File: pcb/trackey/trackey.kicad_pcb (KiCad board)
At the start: 2 copper layers, 53.3 x 58.4 mm, 31 parts, among them J1 trackball_port, J2 Audio-Jack-4, J3 COL_port, J4 ROW_port, J6 has_trackball, J7 is_left, U1 Arduino_Pro_Micro, U2 Arduino_Pro_Micro, U3 MCP23S17

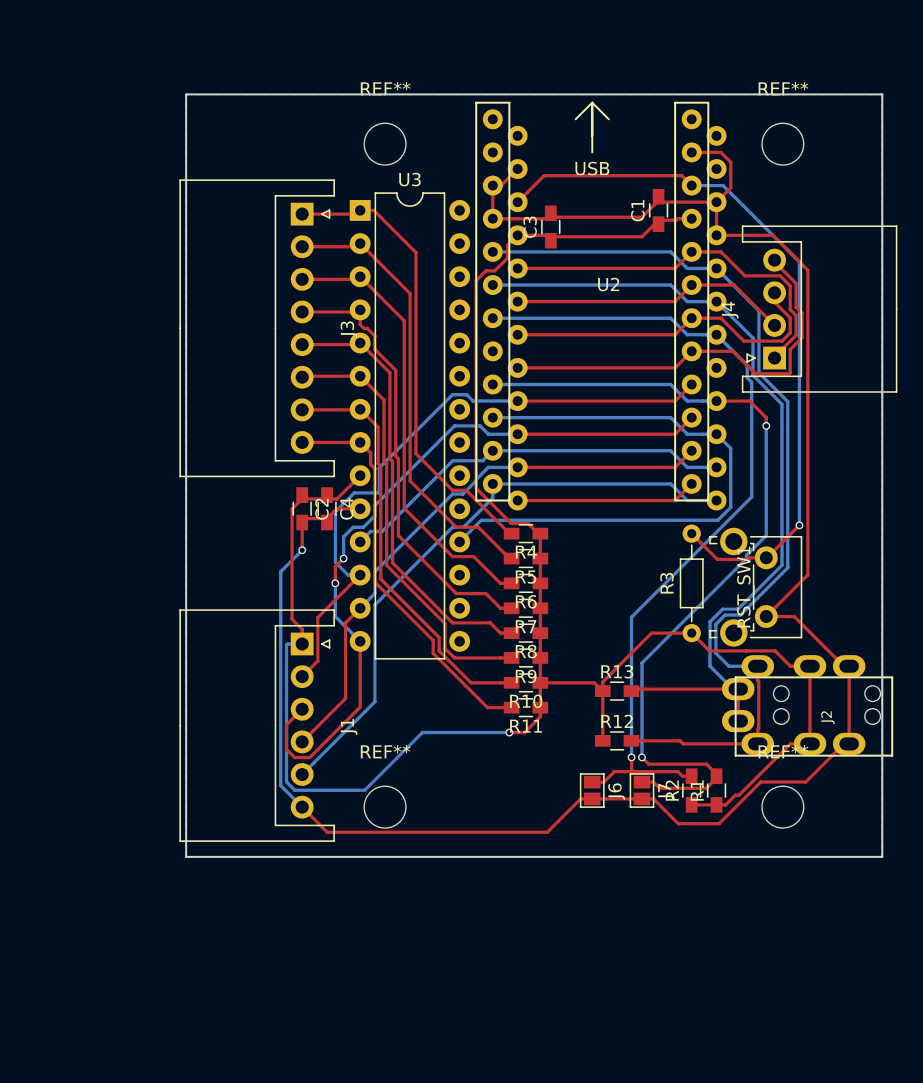
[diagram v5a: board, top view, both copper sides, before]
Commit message: fix mainboard shape
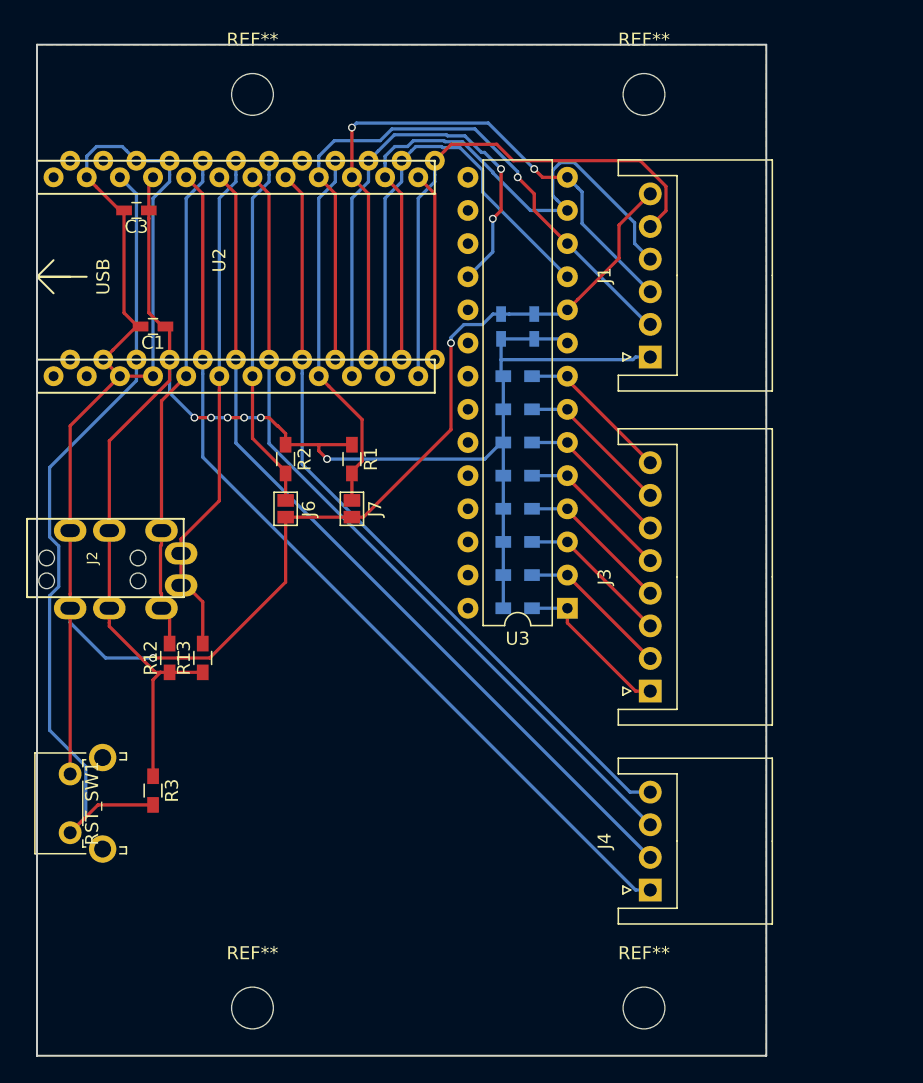
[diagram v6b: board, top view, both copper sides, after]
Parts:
- removed the REF** at (40.6, 3.81)
- removed the REF** at (10.2, 3.81)
- removed the REF** at (40.6, 54.6)
- removed the REF** at (10.2, 54.6)
- added REF**: MountingHole_3.2mm_M3, Mounting_Holes:MountingHole_3.2mm_M3, F.Cu at (0.00, 0.00)
- added REF**: MountingHole_3.2mm_M3, Mounting_Holes:MountingHole_3.2mm_M3, F.Cu at (30.0, 0.00)
- added REF**: MountingHole_3.2mm_M3, Mounting_Holes:MountingHole_3.2mm_M3, F.Cu at (0.00, 70.0)
- added REF**: MountingHole_3.2mm_M3, Mounting_Holes:MountingHole_3.2mm_M3, F.Cu at (30.0, 70.0)
- C1, C3: footprint trackey:R_0603 -> Capacitors_SMD:C_0603_HandSoldering
- C2, C4: footprint trackey:R_0603 -> Capacitors_SMD:C_0603_HandSoldering; moved to B.Cu
- R10, R11, R4, R5, R6, R7, R8, R9: moved to B.Cu
- R3: footprint Resistors_THT:R_Axial_DIN0204_L3.6mm_D1.6mm_P7.62mm_Horizontal -> Resistors_SMD:R_0603_HandSoldering
- moved J2 67.4 mm to (-17.3, 35.5), turned to 90 degrees
- moved RST_SW1 57.3 mm to (-14.0, 56.6), turned to 90 degrees
- moved J3 45.2 mm to (30.5, 45.7), turned to 90 degrees
- moved R3 43.0 mm to (-7.62, 53.3), turned to 270 degrees
- moved J4 41.9 mm to (30.5, 61.0)
- moved R2 40.2 mm to (2.54, 27.9), turned to 270 degrees
- moved C1 39.7 mm to (-7.62, 17.8), turned to 180 degrees
- moved R1 37.8 mm to (7.62, 27.9), turned to 270 degrees
- moved R12 34.9 mm to (-6.35, 43.2), turned to 90 degrees
- moved J1 34.6 mm to (30.5, 20.1), turned to 90 degrees
- moved U3 34.4 mm to (24.1, 39.4), turned to 180 degrees
- moved J6 31.9 mm to (2.54, 31.8)
- moved R13 31.9 mm to (-3.81, 43.2), turned to 90 degrees
- moved C3 31.8 mm to (-8.89, 8.89), turned to 180 degrees
- moved J7 31.0 mm to (7.62, 31.8)
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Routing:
- net /ROW1: track 21.5 -> 65.8 mm
- net /ROW0: track 28.9 -> 70.0 mm
- net /has_trackball: track 64.2 -> 27.6 mm, vias 1 -> 0
- net /is_left: track 64.8 -> 28.3 mm, vias 2 -> 0
- net /ROW2: track 26.0 -> 62.2 mm
- net /SDA: track 71.8 -> 38.6 mm
- net /ROW3: track 32.0 -> 59.6 mm
- net +5V: track 151.1 -> 125.5 mm, vias 1 -> 6
- net /SCL: track 64.2 -> 39.7 mm
- net /COL0: track 35.4 -> 12.3 mm
- net /COL1: track 34.6 -> 11.7 mm
- net /COL2: track 34.3 -> 11.8 mm
- net /COL3: track 34.1 -> 11.8 mm
- net /COL4: track 33.7 -> 11.9 mm
- net /COL5: track 33.4 -> 11.9 mm
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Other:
- board size 53.3 x 58.4 mm -> 55.9 x 77.5 mm

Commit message: improve pcb size
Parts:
- removed C3: 1uF, Capacitors_SMD:C_0603_HandSoldering
- removed C4: 0.1uF, Capacitors_SMD:C_0603_HandSoldering
- removed R10, R11, R6, R7, R8, R9: 10kΩ, Resistors_SMD:R_0603_HandSoldering
- removed R12, R13: 2.2kΩ, Resistors_SMD:R_0603_HandSoldering
- removed the REF** at (30.0, 0.00)
- removed the REF** at (0.00, 70.0)
- removed the REF** at (30.0, 70.0)
- removed U3: MCP23S17, Housings_DIP:DIP-28_W7.62mm
- added J10: is_left, Connectors:GS2, F.Cu at (14.0, 26.0)
- added J11: is_right, Connectors:GS2, B.Cu at (14.0, 26.0)
- added J12: is_left, Connectors:GS2, F.Cu at (16.5, 26.0)
- added J13: is_right, Connectors:GS2, B.Cu at (16.5, 26.0)
- added J14: OLED_conn, Socket_Strips:Socket_Strip_Straight_1x04_Pitch2.54mm, F.Cu at (8.89, 29.2)
- added J5: RJ45, trackey:RJ45_8, B.Cu at (15.2, 34.5)
- added J8: is_left, Connectors:GS2, F.Cu at (11.4, 26.0)
- added J9: is_right, Connectors:GS2, B.Cu at (11.4, 26.0)
- added REF**: MountingHole_3.2mm_M3, Mounting_Holes:MountingHole_3.2mm_M3, F.Cu at (25.4, 0.00)
- added REF**: MountingHole_3.2mm_M3, Mounting_Holes:MountingHole_3.2mm_M3, F.Cu at (0.00, 53.3)
- added REF**: MountingHole_3.2mm_M3, Mounting_Holes:MountingHole_3.2mm_M3, F.Cu at (25.4, 53.3)
- C2, U1: moved to F.Cu
- J2: value Audio-Jack-4 -> RJ45; footprint trackey:MJ-4PP-9_rev2 -> trackey:RJ45_8
- J6: value has_trackball -> is_left
- J7: value is_left -> is_right; moved to B.Cu
- R1, R2: value 2.2kΩ -> 2.2k
- R4, R5: value 10kΩ -> 2.2k; moved to F.Cu
- U2: moved to B.Cu
- moved RST_SW1 64.2 mm to (26.7, 6.93), turned to 270 degrees
- moved R3 54.1 mm to (23.5, 9.14), turned to 90 degrees
- moved J3 49.6 mm to (0.00, 6.63), turned to 270 degrees
- moved J2 33.5 mm to (15.2, 43.4)
- moved J1 29.6 mm to (3.81, 33.0), turned to 270 degrees
- moved C1 29.0 mm to (17.8, 3.81), turned to 90 degrees
- moved R2 25.4 mm to (27.9, 29.2)
- moved J4 22.6 mm to (10.3, 50.8), turned to 0 degrees
- moved R5 18.2 mm to (3.81, 29.2), turned to 180 degrees
- moved C2 18.1 mm to (7.62, 3.81)
- moved R1 17.8 mm to (25.4, 29.2)
- moved R4 16.1 mm to (25.4, 24.1), turned to 180 degrees
- moved U1 15.1 mm to (14.6, 10.2), turned to 0 degrees
- moved U2 12.1 mm to (10.8, 11.4), turned to 180 degrees
- moved J6 8.54 mm to (8.89, 26.0)
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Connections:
- J2 pad 1: /SCL -> +5V
- J2 pad 3: +5V -> /SCL
- J2 pad 4: GND -> /SCLK
- J3 pad 8: /COL7 -> Net-(J3-Pad8)
- J6 pad 1: /has_trackball -> /SDA
- J6 pad 2: GND -> /OLED_1
- J7 pad 1: /is_left -> GND
- J7 pad 2: GND -> /OLED_1
- R1 pad 2: /is_left -> /SCL
- R2 pad 2: /has_trackball -> /SDA
- R4 pad 2: /COL0 -> Net-(R4-Pad2)
- R5 pad 1: +5V -> GND
- R5 pad 2: /COL1 -> Net-(R5-Pad2)
- U1 pad 1: Net-(U1-Pad1) -> /COL0
- U1 pad 10: /Key_IO_RST -> /COL5
- U1 pad 11: /Key_SS -> /COL6
- U1 pad 13: /Arduino_SS -> Net-(R4-Pad2)
- U1 pad 2: Net-(U1-Pad2) -> /COL1
- U1 pad 7: /has_trackball -> /COL2
- U1 pad 8: Net-(U1-Pad8) -> /COL3
- U1 pad 9: /is_left -> /COL4
- U2 pad 1: Net-(U2-Pad1) -> /COL0
- U2 pad 10: /Key_IO_RST -> /COL5
- U2 pad 11: /Key_SS -> /COL6
- U2 pad 13: /Arduino_SS -> Net-(R5-Pad2)
- U2 pad 2: Net-(U2-Pad2) -> /COL1
- U2 pad 7: /has_trackball -> /COL2
- U2 pad 8: Net-(U2-Pad8) -> /COL3
- U2 pad 9: /is_left -> /COL4
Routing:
- net GND: track 149.5 -> 11.3 mm, vias 2 -> 0
- net +5V: track 125.5 -> 12.0 mm, vias 6 -> 0
- net /ROW0: track 70.0 -> 0.00 mm
- net /ROW1: track 65.8 -> 0.00 mm
- net /RST: track 63.0 -> 0.00 mm
- net /ROW2: track 62.2 -> 0.00 mm
- net /ROW3: track 59.6 -> 0.00 mm
- net /SCLK: track 49.6 -> 1.27 mm, vias 1 -> 0
- net /MISO: track 48.1 -> 1.27 mm, vias 2 -> 0
- net /MOSI: track 48.1 -> 5.49 mm
- net /Key_IO_RST: track 38.4 -> 0.00 mm, vias 2 -> 0
- net /Key_SS: track 35.3 -> 0.00 mm
- net /SCL: track 39.7 -> 5.49 mm
- net /Trackball_SS: track 40.2 -> 8.41 mm
- net /SDA: track 38.6 -> 8.41 mm
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- removed copper zone on B.Cu, net GND
- removed copper zone on F.Cu, net GND
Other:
- board size 55.9 x 77.5 mm -> 33 x 63.5 mm

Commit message: wiring
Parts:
- moved R3 8.02 mm to (26.7, 16.5)
- moved R1 2.54 mm to (25.4, 26.7)
- moved R2 2.54 mm to (27.9, 26.7)
- moved R4 1.80 mm to (26.7, 22.9)
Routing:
- net GND: track 11.3 -> 139.8 mm, vias 0 -> 5
- net +5V: track 12.0 -> 114.4 mm, vias 0 -> 3
- net /SDA: track 8.41 -> 88.6 mm, vias 0 -> 1
- net /ROW0: track 0.00 -> 72.6 mm
- net /ROW1: track 0.00 -> 71.8 mm
- net /ROW2: track 0.00 -> 71.1 mm
- net /ROW3: track 0.00 -> 70.3 mm
- net /MISO: track 1.27 -> 70.3 mm
- net /SCL: track 5.49 -> 73.3 mm, vias 0 -> 3
- net /Trackball_SS: track 8.41 -> 66.5 mm, vias 0 -> 1
- net /SCLK: track 1.27 -> 57.2 mm
- net /MOSI: track 5.49 -> 52.8 mm
- net /RST: track 0.00 -> 35.7 mm
- net /COL0: track 0.00 -> 28.2 mm
- net /COL1: track 0.00 -> 28.2 mm
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- added copper zone on B.Cu, net GND
- added copper zone on F.Cu, net GND
